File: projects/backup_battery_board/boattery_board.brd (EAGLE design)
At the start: 61 x 68 mm, 7 parts, among them X1 22-23-2021

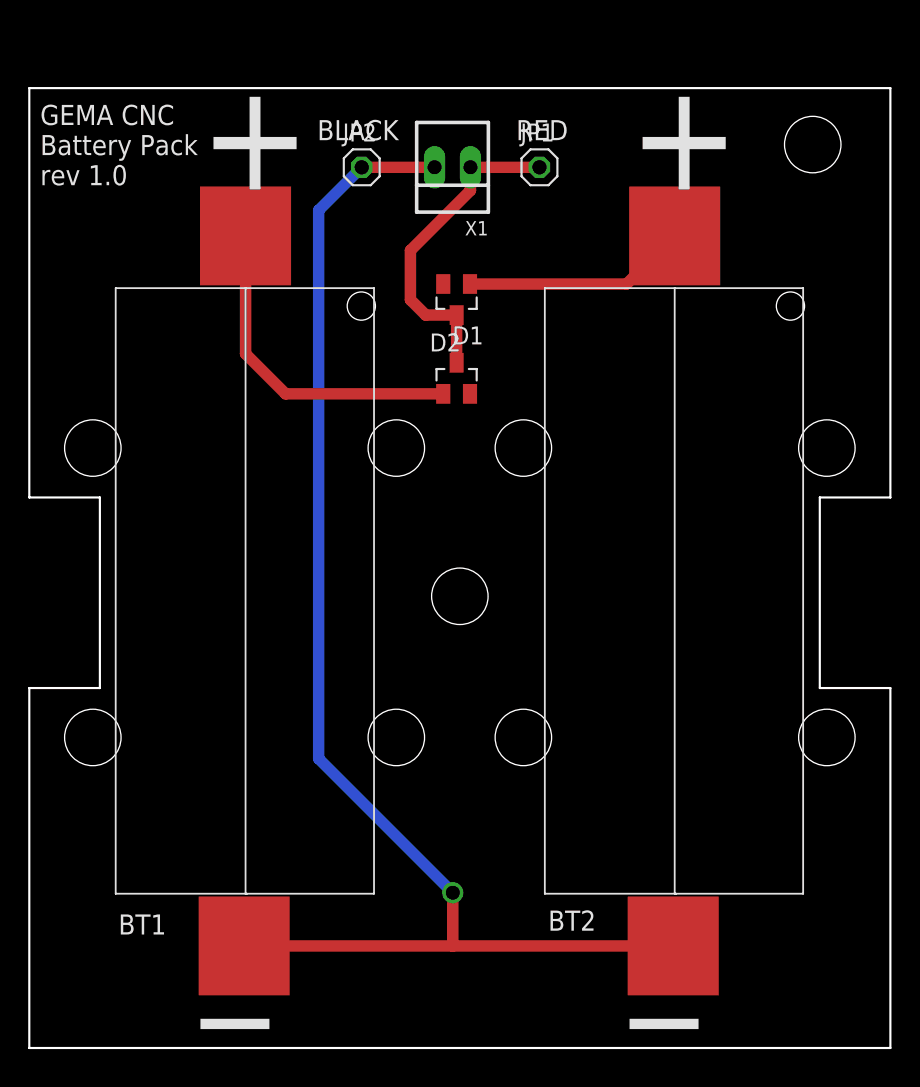
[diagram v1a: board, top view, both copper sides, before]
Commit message: updated battery board
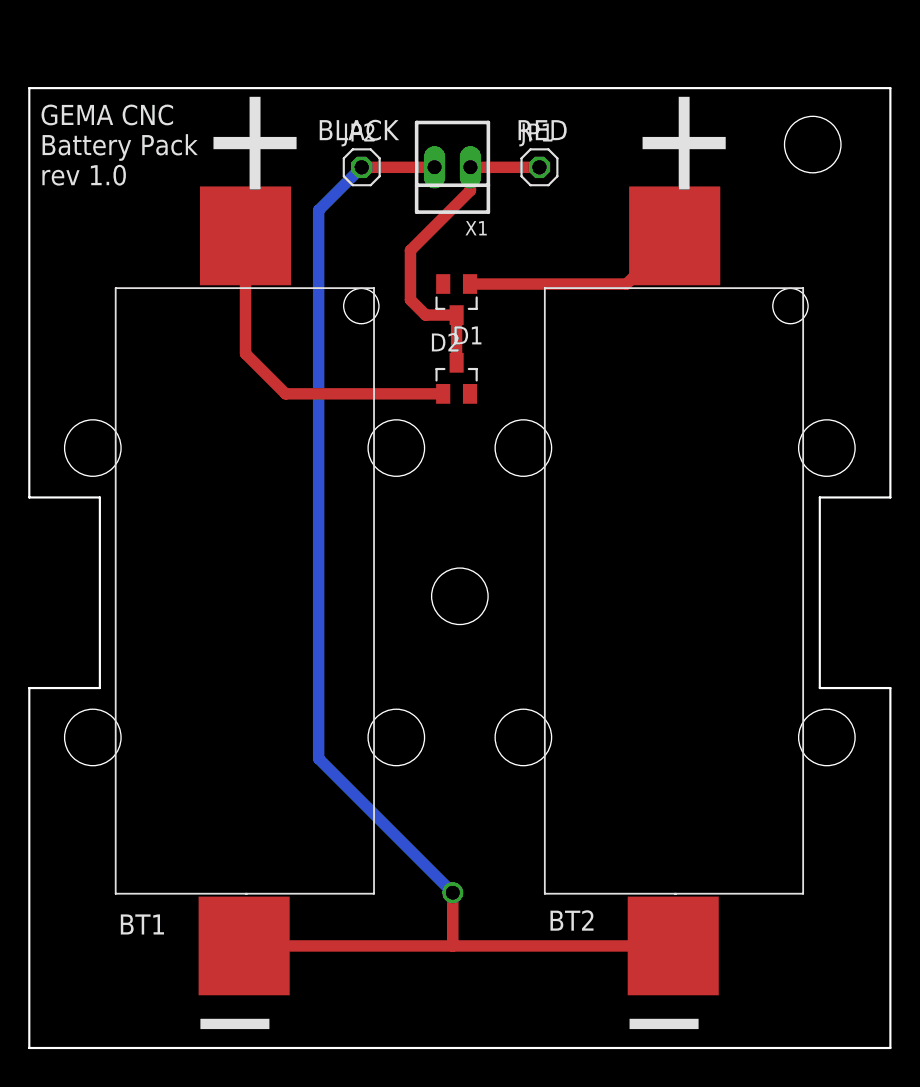
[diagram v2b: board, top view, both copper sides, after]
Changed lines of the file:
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@@
 <layers>
 <layer number="1" name="Top" color="4" fill="1" visible="yes" active="yes"/>
+<layer number="2" name="Route2" color="1" fill="3" visible="no" active="no"/>
+<layer number="3" name="Route3" color="4" fill="3" visible="no" active="no"/>
+<layer number="4" name="Route4" color="1" fill="4" visible="no" active="no"/>
+<layer number="5" name="Route5" color="4" fill="4" visible="no" active="no"/>
+<layer number="6" name="Route6" color="1" fill="8" visible="no" active="no"/>
+<layer number="7" name="Route7" color="4" fill="8" visible="no" active="no"/>
+<layer number="8" name="Route8" color="1" fill="2" visible="no" active="no"/>
+<layer number="9" name="Route9" color="4" fill="2" visible="no" active="no"/>
+<layer number="10" name="Route10" color="1" fill="7" visible="no" active="no"/>
+<layer number="11" name="Route11" color="4" fill="7" visible="no" active="no"/>
+<layer number="12" name="Route12" color="1" fill="5" visible="no" active="no"/>
+<layer number="13" name="Route13" color="4" fill="5" visible="no" active="no"/>
+<layer number="14" name="Route14" color="1" fill="6" visible="no" active="no"/>
+<layer number="15" name="Route15" color="4" fill="6" visible="no" active="no"/>
 <layer number="16" name="Bottom" color="1" fill="1" visible="yes" active="yes"/>
 <layer number="17" name="Pads" color="2" fill="1" visible="yes" active="yes"/>
